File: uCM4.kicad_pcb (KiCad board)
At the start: 2 copper layers, 55 x 48 mm, 81 parts, among them IC1 MAX17048G+, J10 USB_C_Receptacle, J2 Micro_SD_Card_Det, J4 Conn_01x04, J5 DummyJ, J6 DummyJ, Q2 SI2369DS, U1 BNO055, U18 RT9742GGJ5, U2 SN74LVC1G07DBVR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

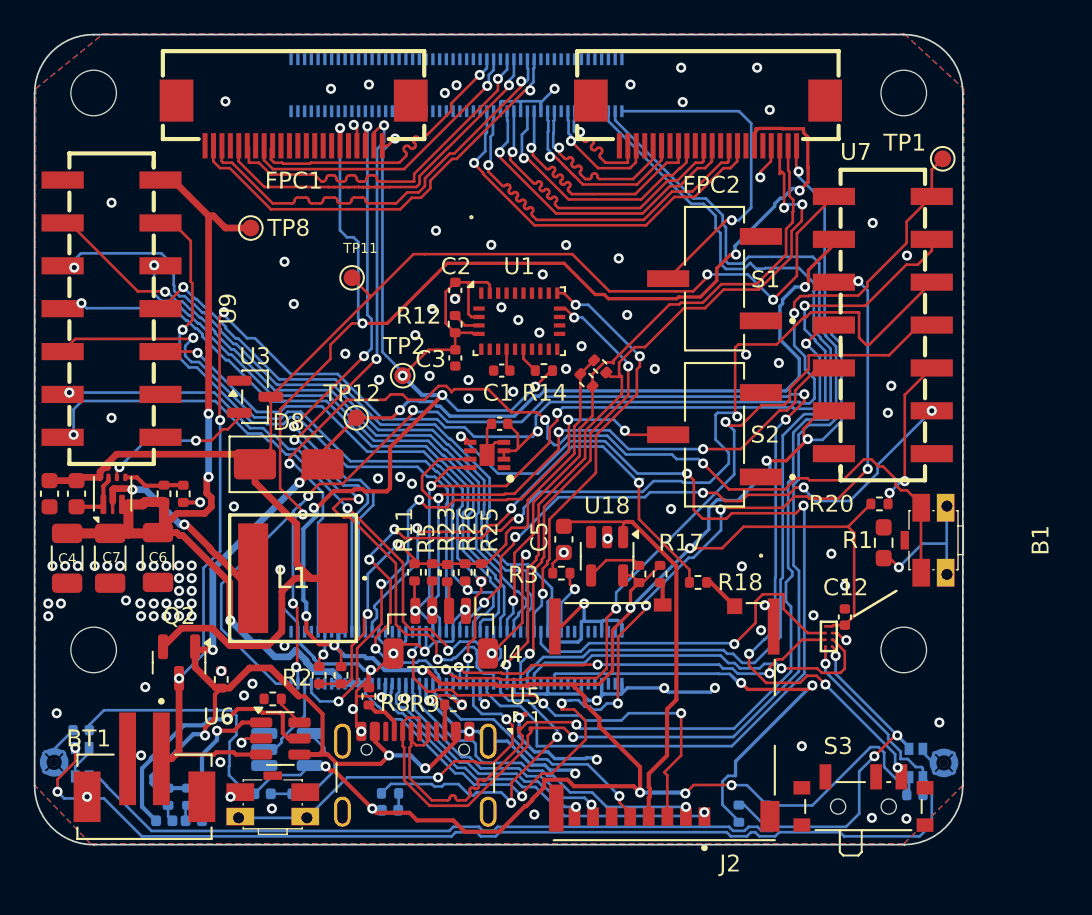
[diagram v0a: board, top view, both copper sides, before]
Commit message: Routed first camera (with proper length matching this time)
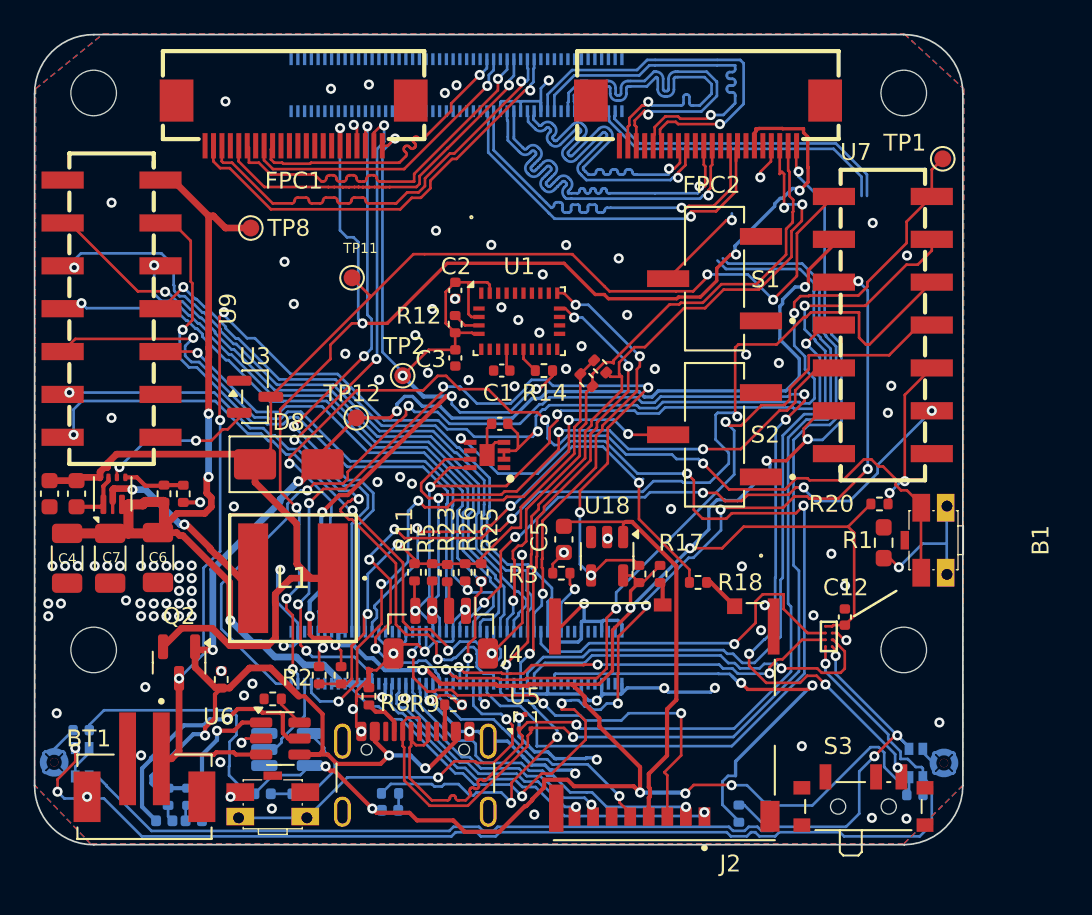
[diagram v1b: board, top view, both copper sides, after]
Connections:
- Module1 pad 75: unconnected-(Module1A-SD_PWR_ON-Pad75) -> /SD_PWR_ON
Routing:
- net /SD_PWR_ON: track 3.34 -> 55.4 mm, vias 0 -> 7
- net /CAM1_D0_P: track 7.37 -> 22.9 mm
- net /CAM1_D0_N: track 7.34 -> 22.9 mm
- net Net-(Module1B-USB_OTG_ID): track 19.6 -> 5.61 mm
- net /CAM1_D1_N: track 11.4 -> 22.6 mm
- net /CAM1_D1_P: track 11.4 -> 22.6 mm
- net /CAM1_C_P: track 15.4 -> 22.6 mm
- net /CAM1_C_N: track 15.4 -> 22.5 mm
- net /USB_P: track 77.7 -> 83.1 mm
- net /USB_N: track 78.1 -> 83.4 mm
- net GND: track 125.0 -> 120.7 mm, vias 127 -> 121
- net /CAM1_D2_P: track 19.0 -> 22.9 mm
- net /CAM1_D2_N: track 18.9 -> 22.8 mm
- net Net-(Module1A-Global_EN): track 78.7 -> 79.9 mm
- net +3V3: track 225.8 -> 224.6 mm
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
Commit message: Second camera routed (with proper trace lengths this time!)
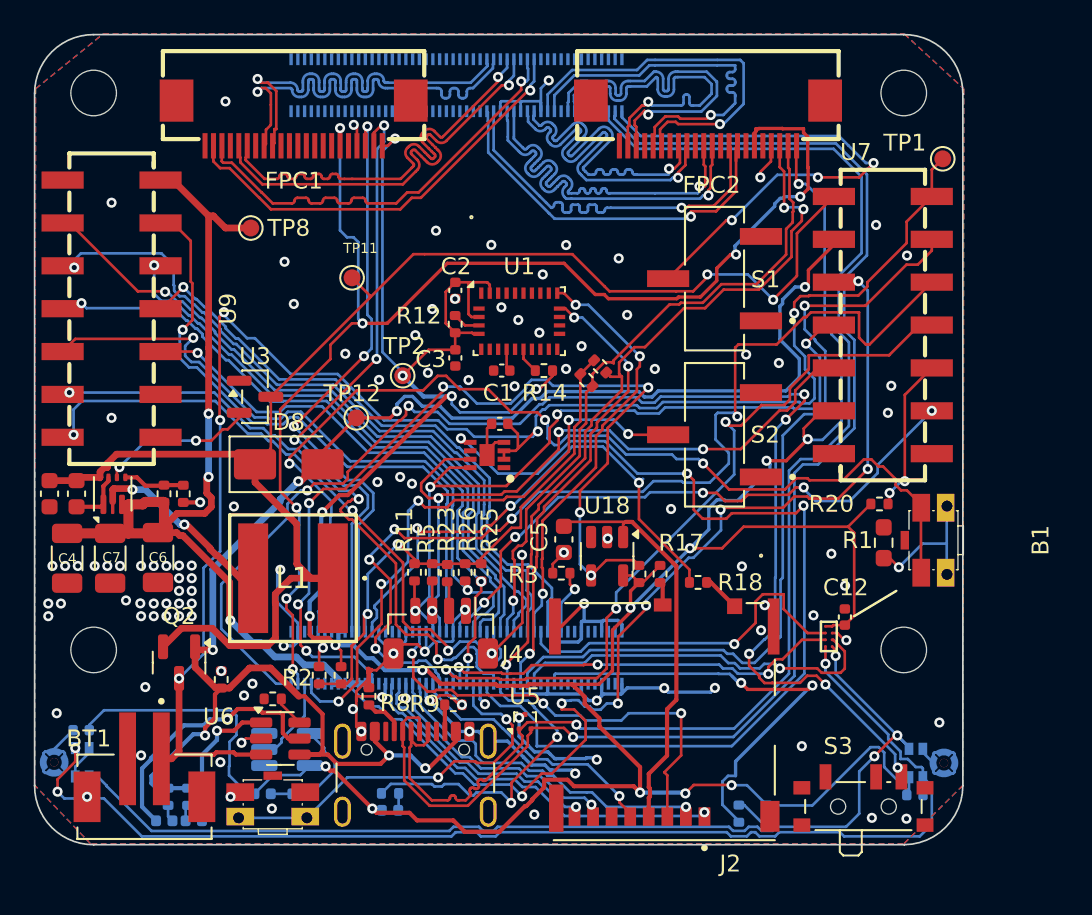
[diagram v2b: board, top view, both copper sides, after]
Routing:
- net Net-(Module1B-USB_OTG_ID): track 5.61 -> 31.5 mm, vias 1 -> 3
- net /CAM0_C_N: track 18.0 -> 28.1 mm
- net /CAM0_C_P: track 18.0 -> 25.6 mm
- net /CAM0_D1_N: track 22.0 -> 25.7 mm
- net /CAM0_D1_P: track 22.0 -> 25.6 mm
- net /USB_N: track 83.4 -> 82.5 mm
- net /USB_P: track 83.1 -> 82.5 mm
- net GND: vias 121 -> 117

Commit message: DRC checked.
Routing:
- net GND: track 120.7 -> 129.0 mm, vias 117 -> 129
- net /CAM1_C_N: track 22.5 -> 25.4 mm
- net /CAM_GPIO: track 78.6 -> 80.0 mm

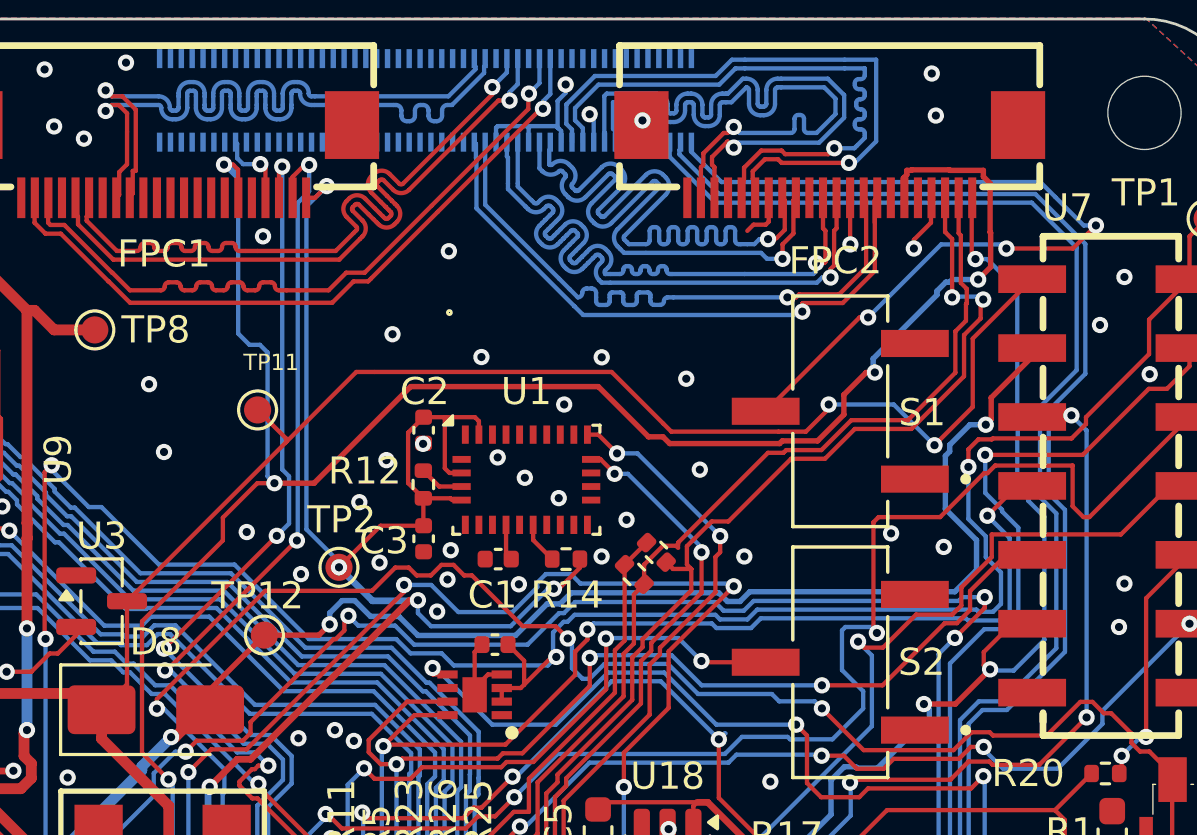
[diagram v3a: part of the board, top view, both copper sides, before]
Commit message: Switched camera I2Cs to match official RPi documentation.
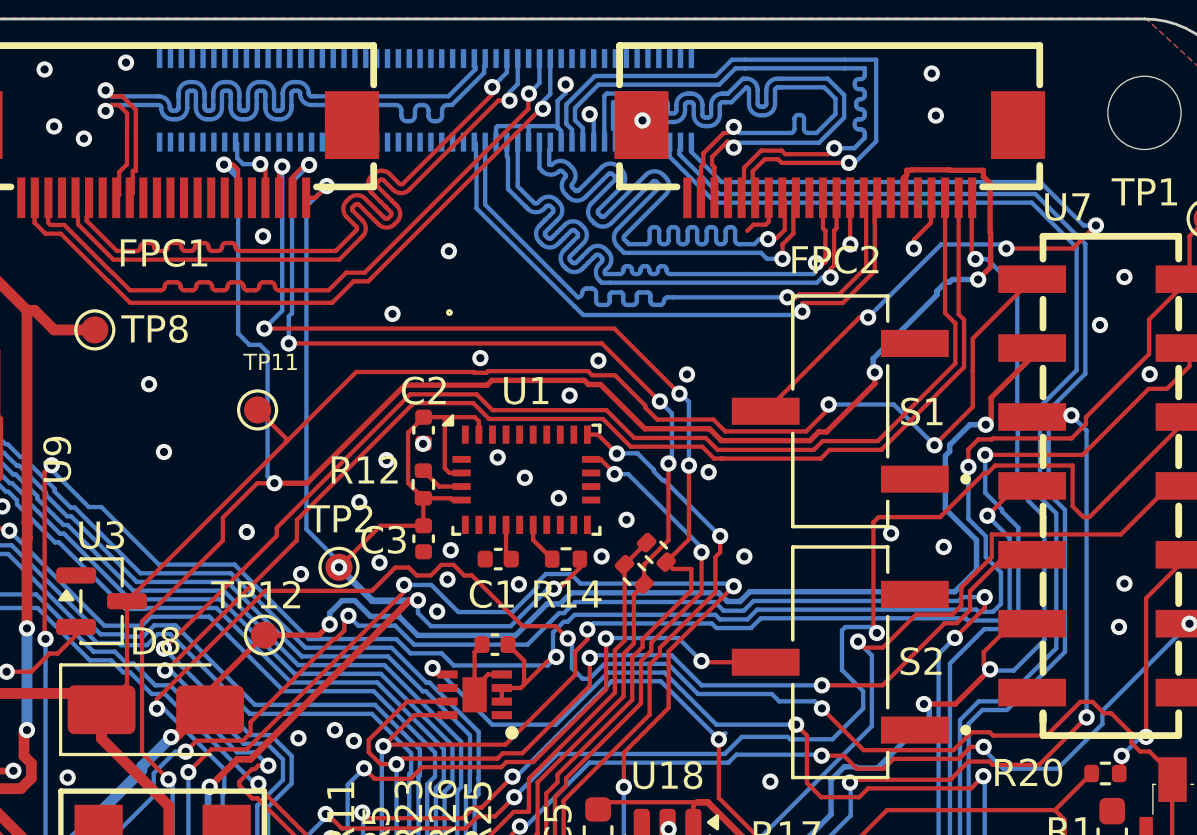
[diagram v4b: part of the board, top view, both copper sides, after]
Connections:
- FPC1 pad 2: /SDA0 -> /SDA1
- FPC1 pad 3: /SCL0 -> /SCL1
- FPC2 pad 2: /SDA1 -> /SDA0
- FPC2 pad 3: /SCL1 -> /SCL0
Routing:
- net /SCL0: track 35.9 -> 56.6 mm, vias 3 -> 1
- net /SDA0: track 36.6 -> 56.7 mm, vias 3 -> 1
- net /SCL1: track 43.9 -> 52.5 mm, vias 3 -> 5
- net /SDA1: track 38.8 -> 47.2 mm, vias 1 -> 5

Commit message: Production ready files.
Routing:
- net /CAM1_D3_P: track 23.2 -> 22.4 mm
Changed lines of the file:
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@@
 			)
 		)
-		(property "LCSC Part" "C42163135"
+		(property "LCSC Part #" "C42163135"
 			(at 0 0 90)
 			(unlocked yes)
@@
 		(sheetname "/")
 		(sheetfile "uCM4.kicad_sch")
-		(attr exclude_from_pos_files)
+		(attr exclude_from_pos_files exclude_from_bom)
 		(fp_circle
 			(center 0 0)
@@
 		(sheetname "/")
 		(sheetfile "uCM4.kicad_sch")
-		(attr exclude_from_pos_files)
+		(attr exclude_from_pos_files exclude_from_bom)
 		(fp_circle
 			(center 0 0)
@@
 			)
 		)
-		(property "LCSC Part" "C42163135"
+		(property "LCSC Part #" "C42163135"
 			(at 0 0 270)
 			(unlocked yes)
@@
 		(sheetname "/")
 		(sheetfile "uCM4.kicad_sch")
-		(attr exclude_from_pos_files)
+		(attr exclude_from_pos_files exclude_from_bom)
 		(fp_circle
 			(center 0 0)
@@
 		(sheetname "/")
 		(sheetfile "uCM4.kicad_sch")
-		(attr exclude_from_pos_files)
+		(attr exclude_from_pos_files exclude_from_bom)
 		(fp_circle
 			(center 0 0)
@@
 		(sheetname "/")
 		(sheetfile "uCM4.kicad_sch")
-		(attr exclude_from_pos_files)
+		(attr exclude_from_pos_files exclude_from_bom)
 		(fp_circle
 			(center 0 0)
@@
 			)
 		)
-		(property "LCSC#" "C424649"
+		(property "LCSC#" "C597931"
+			(at 0 0 180)
+			(unlocked yes)
+			(layer "B.Fab")
+			(hide yes)
+			(effects
+				(font
+					(size 1 1)
+					(thickness 0.15)
+				)
+				(justify mirror)
+			)
+		)
+		(property "LCSC Part #" "C597931"
 			(at 0 0 180)
 			(unlocked yes)
@@
 			)
 		)
-		(property "LCSC#" "C424649"
+		(property "LCSC#" "C597931"
+			(at 0 0 180)
+			(unlocked yes)
+			(layer "B.Fab")
+			(hide yes)
+			(effects
+				(font
+					(size 1 1)
+					(thickness 0.15)
+				)
+				(justify mirror)
+			)
+		)
+		(property "LCSC Part #" "C597931"
 			(at 0 0 180)
 			(unlocked yes)
@@
 		(sheetname "/")
 		(sheetfile "uCM4.kicad_sch")
-		(attr smd exclude_from_pos_files)
+		(attr smd exclude_from_pos_files exclude_from_bom)
 		(fp_line
 			(start 0 -3.5)
@@
 		(width 0.16)
 		(layer "F.Cu")
-		(net 33)
-	)
-	(segment
-		(start 162.5 92.55)
-		(end 162.5 91.72)
-		(width 0.16)
-		(layer "F.Cu")
